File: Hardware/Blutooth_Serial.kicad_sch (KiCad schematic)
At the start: 7 parts, among them J1 Test_Pad, U2 LM2596S-3.3

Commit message: code changes
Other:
- moved on the sheet: C1, C2, D2, J1, L1, U2

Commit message: updated schematic
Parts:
- removed U2: LM2596S-3.3, Package_TO_SOT_SMD:TO-263-5_TabPin3, symbol Regulator_Switching:LM2596S-3.3
- added C3: 0.1uF, Capacitor_SMD:C_0805_2012Metric, symbol Device:C
- added C4, C5, C6: 0.47uF, Capacitor_SMD:C_0805_2012Metric, symbol Device:C
- added C7: 0.1uF, symbol Device:C
- added J2: DE9_Receptacle_MountingHoles, Connector_Dsub:DSUB-9_Female_Horizontal_P2.77x2.84mm_EdgePinOffset4.94mm_Housed_MountingHolesOffset7.48mm, symbol Connector:DE9_Receptacle_MountingHoles
- added JP1, JP2, JP3, JP4, JP5, JP6, JP7, JP8, JP9: SolderJumper_2_Open, Jumper:SolderJumper-2_P1.3mm_Open_Pad1.0x1.5mm, symbol Jumper:SolderJumper_2_Open
- added U2: MAX3232, Package_DIP:DIP-16_W8.89mm_SMDSocket_LongPads, symbol Interface_UART:MAX3232
- added U3: LM2596S-5, Package_TO_SOT_SMD:TO-263-5_TabPin3, symbol Regulator_Switching:LM2596S-5
- C1: value 150uF -> 470uF
- C2: value 680uF -> 220uF; footprint Capacitor_THT:C_Radial_D12.5mm_H25.0mm_P5.00mm -> Capacitor_THT:C_Radial_D10.0mm_H16.0mm_P5.00mm
- L1: value 33uH -> 68uH
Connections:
- net +24V: now also U3.1 (VIN)
- net GND: now also C4.2, C6.2, C7.2, J2.5, U2.15 (GND), U3.3 (GND)
- net at D2.1 (K), L1.1: now also U3.2 (OUT)
- net at J1.1 (Pin_1): now also U3.5 (~{ON}/OFF)
- net T1IN: now reaches IC1.4 (TXD)
- net T1IN: now also JP5.1 (A)
- net R1OUT: now reaches IC1.5 (RXD)
- net R1OUT: now also JP7.1 (A)
- net 3.3V renamed 5V
- net 5V: now also C7.1, JP9.1 (A), U2.16 (VCC), U3.4 (FB); no longer IC1.2 (Vcc)
- new net: C5.1, U2.4 (C2+)
- new net: C5.2, U2.5 (C2-)
- new net: C3.1, U2.1 (C1+)
- new net: JP6.2 (B), U2.10 (T2IN)
- new net: JP5.2 (B), U2.11 (T1IN)
- new net: JP7.2 (B), U2.12 (R1OUT)
- new net: JP3.1 (A), U2.13 (R1IN)
- new net: JP1.1 (A), U2.14 (T1OUT)
- new net: C4.1, U2.2 (VS+)
- new net: C3.2, U2.3 (C1-)
- new net: C6.1, U2.6 (VS-)
- new net: JP2.1 (A), U2.7 (T2OUT)
- new net: JP4.1 (A), U2.8 (R2IN)
- new net: JP8.2 (B), U2.9 (R2OUT)
- new net: IC1.2 (Vcc), JP9.2 (B)
- new net R1IN: J2.3, JP3.2 (B)
- new net R2IN: JP4.2 (B)
- new net R2OUT: JP8.1 (A)
- new net T1OUT: J2.2, JP1.2 (B)
- new net T2IN: JP6.1 (A)
- new net T2OUT: JP2.2 (B)
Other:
- note added: "R232 Transciever"
- moved on the sheet: IC1

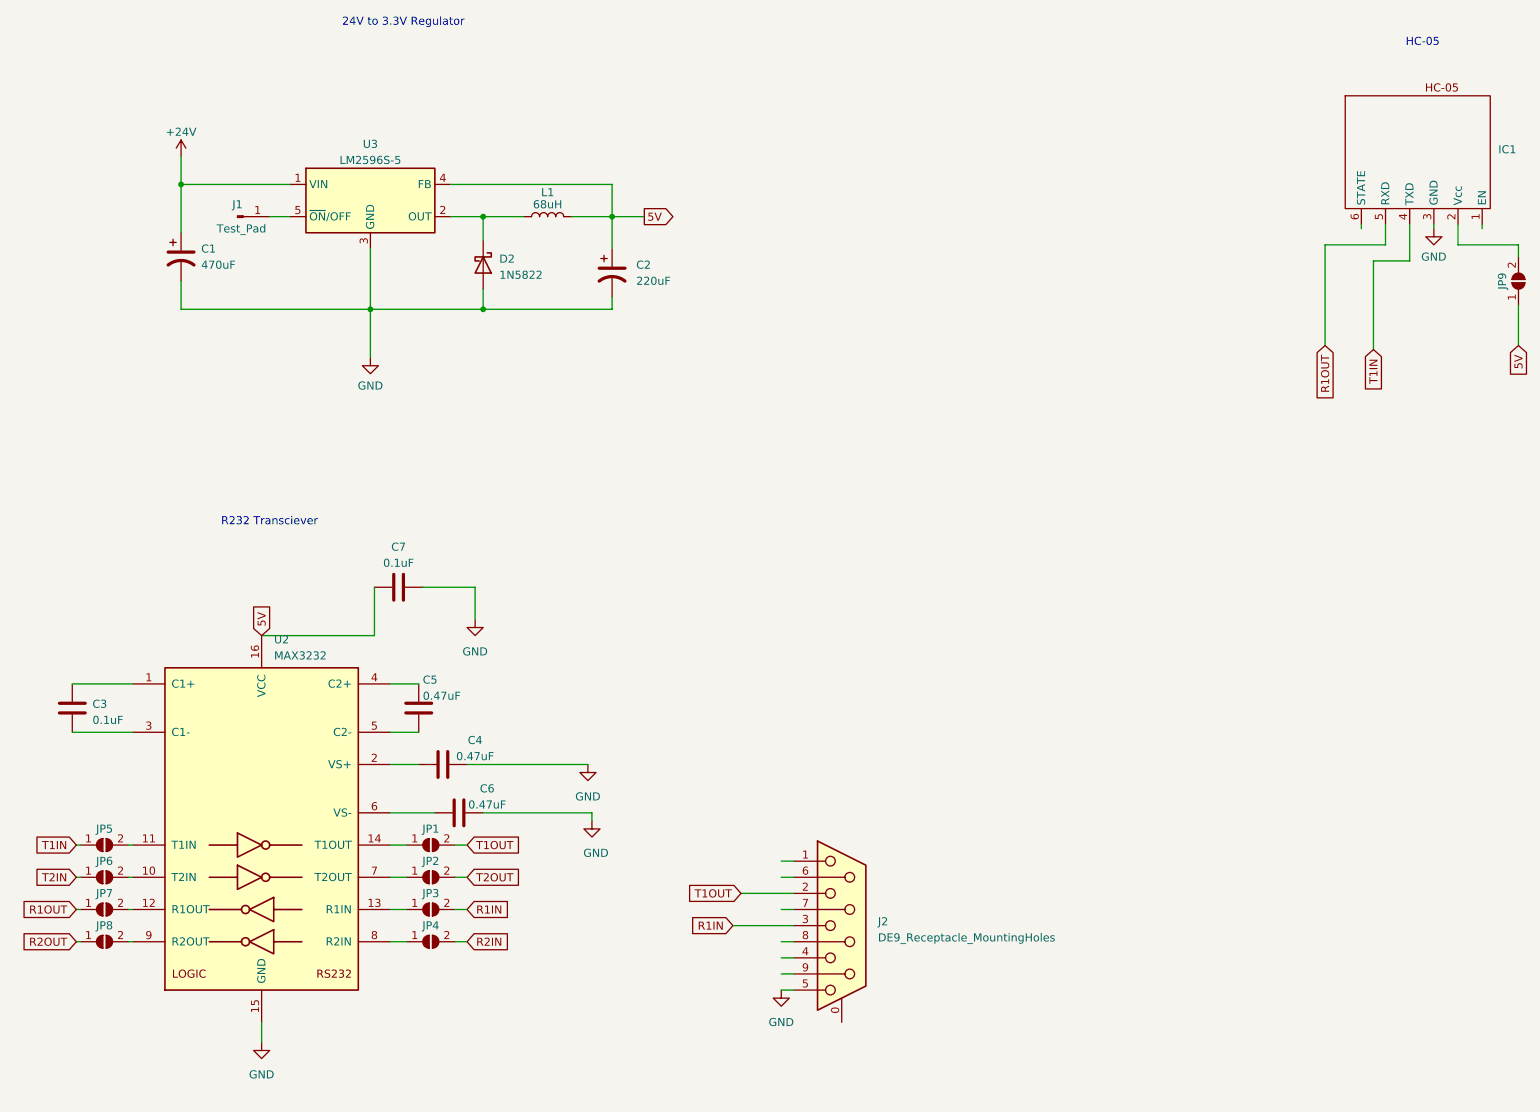
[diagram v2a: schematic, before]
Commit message: reorganized and switched components
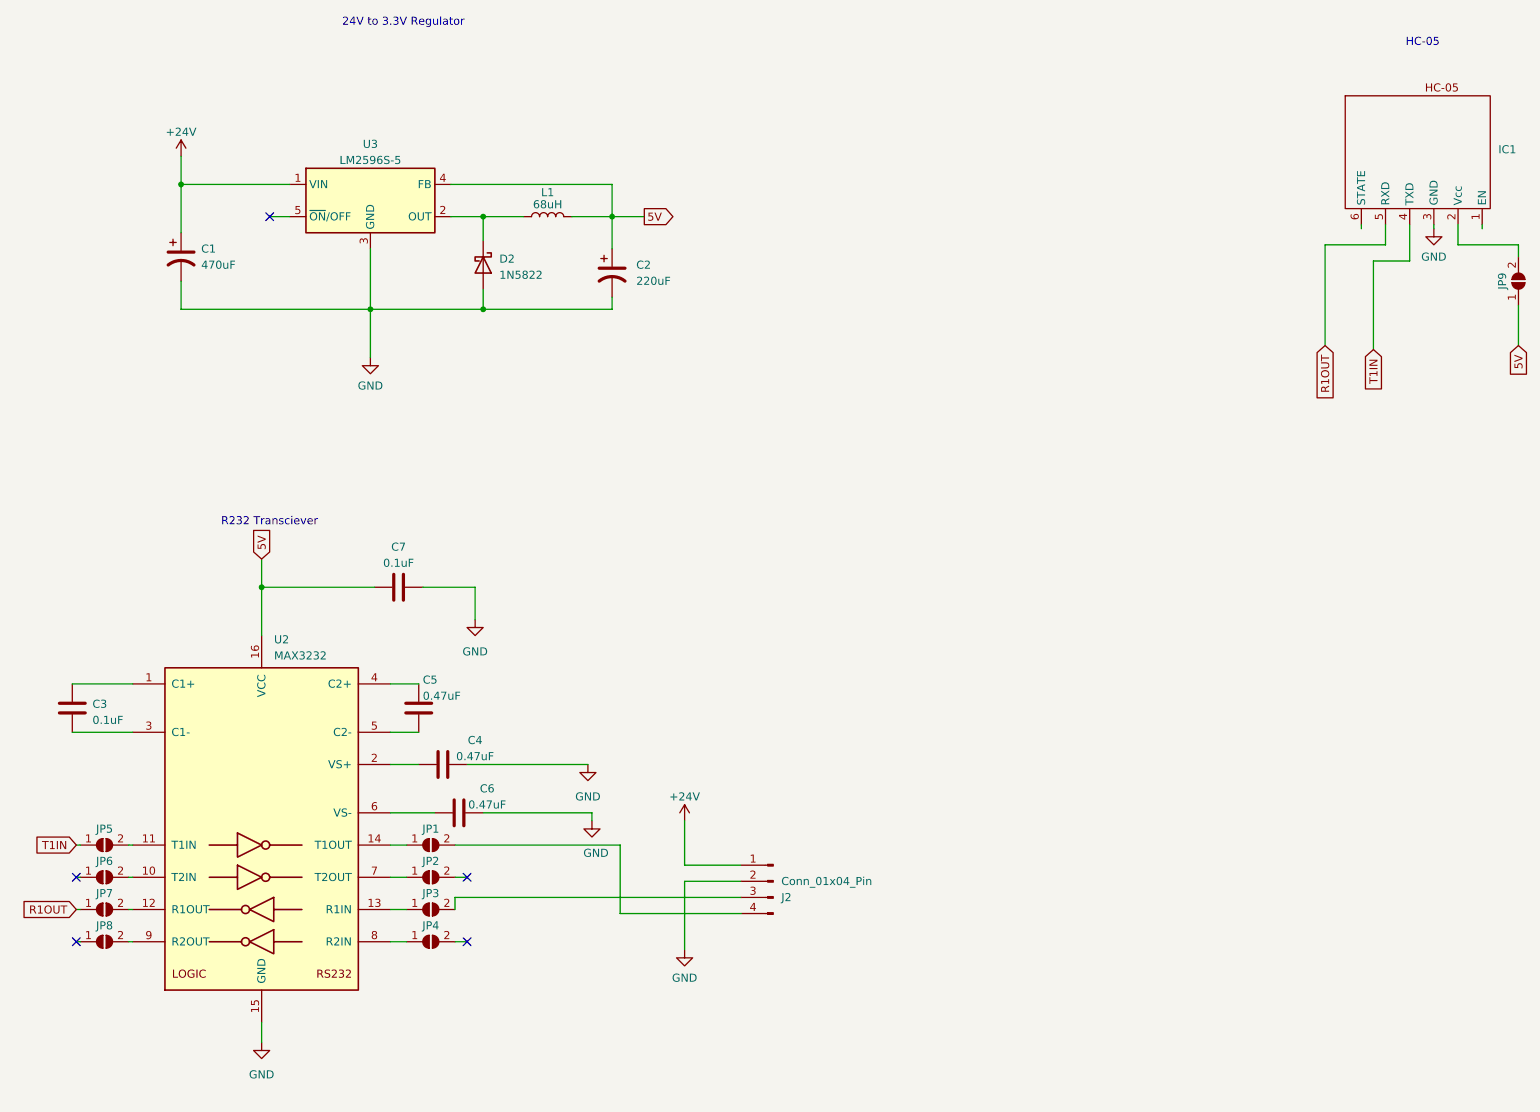
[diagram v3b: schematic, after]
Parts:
- removed J1: Test_Pad, Connector_PinHeader_2.54mm:PinHeader_1x01_P2.54mm_Vertical, symbol Connector:Conn_01x01_Pin
- removed J2: DE9_Receptacle_MountingHoles, Connector_Dsub:DSUB-9_Female_Horizontal_P2.77x2.84mm_EdgePinOffset4.94mm_Housed_MountingHolesOffset7.48mm, symbol Connector:DE9_Receptacle_MountingHoles
- added J2: Conn_01x04_Pin, my_lib:male_pin_4, symbol Connector:Conn_01x04_Pin
- C1: footprint Capacitor_THT:C_Radial_D10.0mm_H16.0mm_P5.00mm -> my_lib:470uF_SMD_CAP
- C2: footprint Capacitor_THT:C_Radial_D10.0mm_H16.0mm_P5.00mm -> my_lib:220uF_SMD_CAP
- C7: footprint (none) -> Capacitor_SMD:C_0805_2012Metric
- D2: footprint Diode_THT:D_DO-201AD_P15.24mm_Horizontal -> Diode_SMD:D_0805_2012Metric
- U2: footprint Package_DIP:DIP-16_W8.89mm_SMDSocket_LongPads -> my_lib:MAX3232EIDR
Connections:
- net +24V: now also J2.1 (Pin_1)
- net GND: now also J2.2 (Pin_2)
- net R1IN: no longer names the net of JP3.2 (B)
- net R1IN: now also J2.3 (Pin_3)
- net R2IN: no longer names the net of JP4.2 (B)
- net R2OUT: no longer names the net of JP8.1 (A)
- net T1OUT: no longer names the net of JP1.2 (B)
- net T1OUT: now also J2.4 (Pin_4)
- net T2IN: no longer names the net of JP6.1 (A)
- net T2OUT: no longer names the net of JP2.2 (B)
- no-connect marks 0 -> 5

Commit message: changes
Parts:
- C1: renamed from C2; footprint my_lib:220uF_SMD_CAP -> Library:220uF_SMD_CAP
- C2: renamed from C7; footprint Capacitor_SMD:C_0805_2012Metric -> Library:C_0805_2012Metric
- C3, C4, C5, C6: footprint Capacitor_SMD:C_0805_2012Metric -> Library:C_0805_2012Metric
- C7: renamed from C1; footprint my_lib:470uF_SMD_CAP -> Library:470uF_SMD_CAP
- D1: renamed from D2; footprint Diode_SMD:D_0805_2012Metric -> Library:D_0805_2012Metric
- IC1: footprint my_lib:HC-05 -> Library:HC-05
- J1: renamed from J2; footprint my_lib:male_pin_4 -> Library:male_pin_4
- JP1: renamed from JP9; footprint Jumper:SolderJumper-2_P1.3mm_Open_Pad1.0x1.5mm -> Library:SolderJumper-2_P1.3mm_Open_Pad1.0x1.5mm
- JP2: renamed from JP1; footprint Jumper:SolderJumper-2_P1.3mm_Open_Pad1.0x1.5mm -> Library:SolderJumper-2_P1.3mm_Open_Pad1.0x1.5mm
- JP3, JP5, JP6: footprint Jumper:SolderJumper-2_P1.3mm_Open_Pad1.0x1.5mm -> Library:SolderJumper-2_P1.3mm_Open_Pad1.0x1.5mm
- JP4: renamed from JP7; footprint Jumper:SolderJumper-2_P1.3mm_Open_Pad1.0x1.5mm -> Library:SolderJumper-2_P1.3mm_Open_Pad1.0x1.5mm
- JP7: renamed from JP2; footprint Jumper:SolderJumper-2_P1.3mm_Open_Pad1.0x1.5mm -> Library:SolderJumper-2_P1.3mm_Open_Pad1.0x1.5mm
- JP8: renamed from JP4; footprint Jumper:SolderJumper-2_P1.3mm_Open_Pad1.0x1.5mm -> Library:SolderJumper-2_P1.3mm_Open_Pad1.0x1.5mm
- JP9: renamed from JP8; footprint Jumper:SolderJumper-2_P1.3mm_Open_Pad1.0x1.5mm -> Library:SolderJumper-2_P1.3mm_Open_Pad1.0x1.5mm
- L1: footprint my_lib:L_12x12mm_H6mm -> Library:L_12x12mm_H6mm
- U1: renamed from U3; footprint Package_TO_SOT_SMD:TO-263-5_TabPin3 -> Library:TO-263-5_TabPin3
- U2: footprint my_lib:MAX3232EIDR -> Library:MAX3232EIDR
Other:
- company: (none) -> Secured Solutions Group
- title: (none) -> Blutooth Serial
- moved on the sheet: C2, C3, C4, C5, C6, J1, JP2, JP3, JP4, JP5, JP6, JP7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
